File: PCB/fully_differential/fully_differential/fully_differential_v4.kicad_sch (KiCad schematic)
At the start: 35 parts, among them J1 Conn_01x02, J2 Conn_01x03, J3 Conn_01x03, U1 LM324, U2 LM324, U3 LM358, U4 AD8138ARZ, U5 L7805, U6 L7905

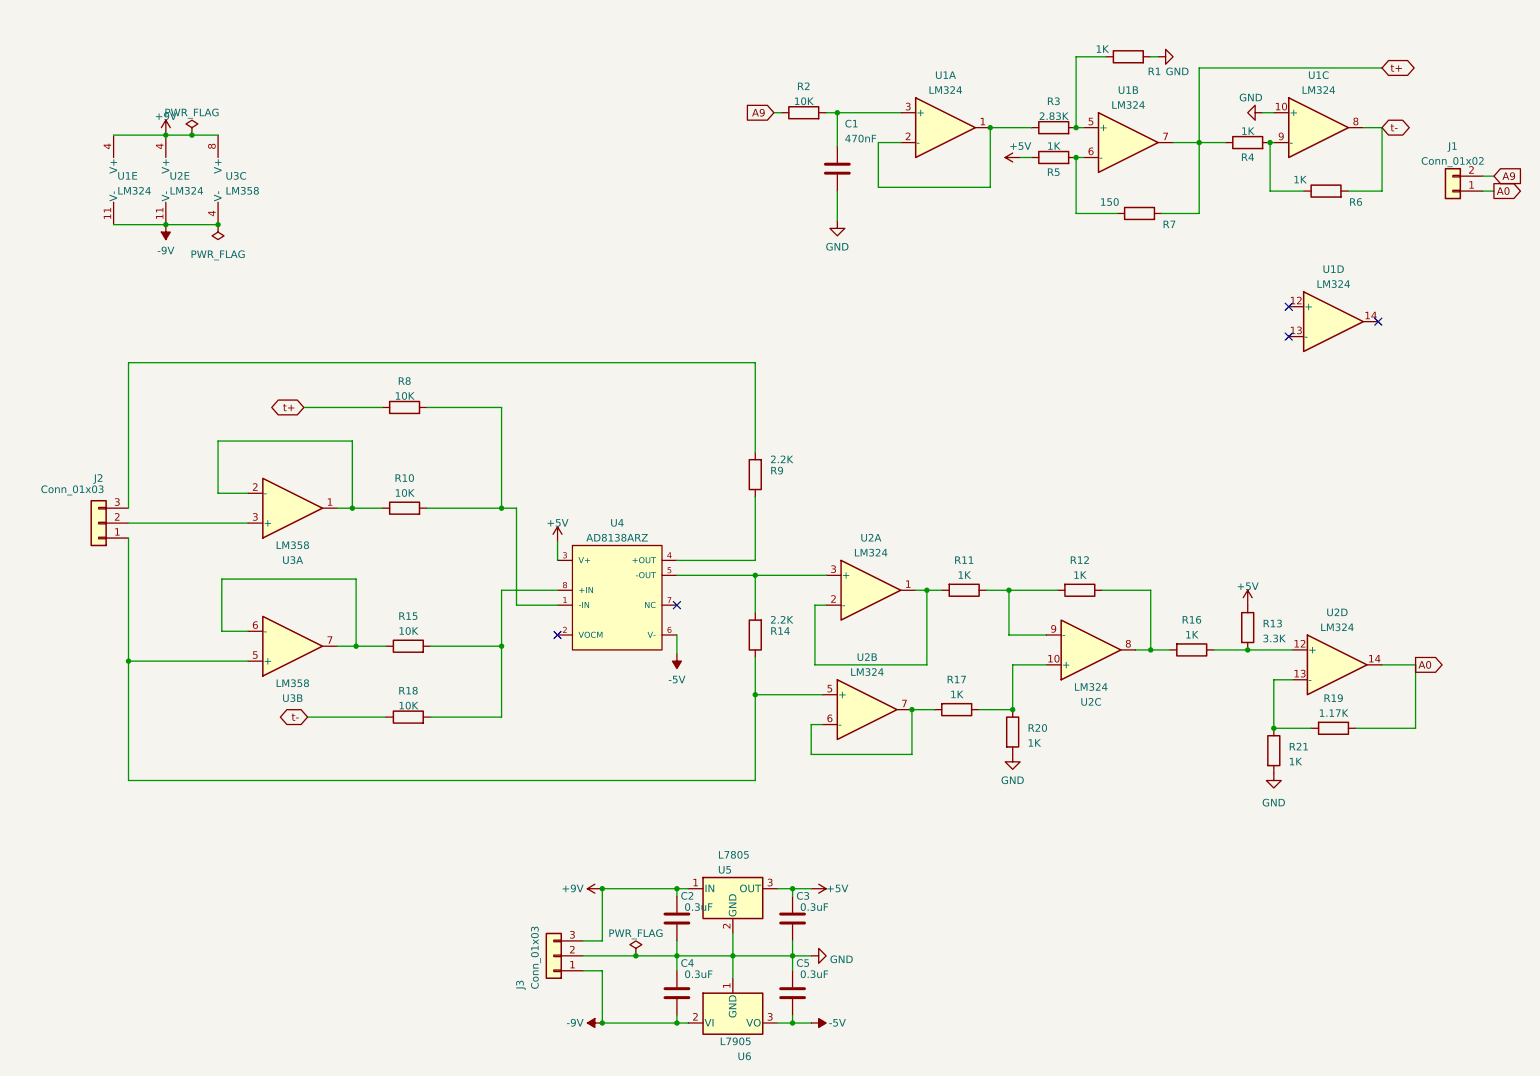
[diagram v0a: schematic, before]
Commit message: fix proteus 1.5v and 3v
stock v2 proteus and kicad ok
fully v4 proteus and kicad ok
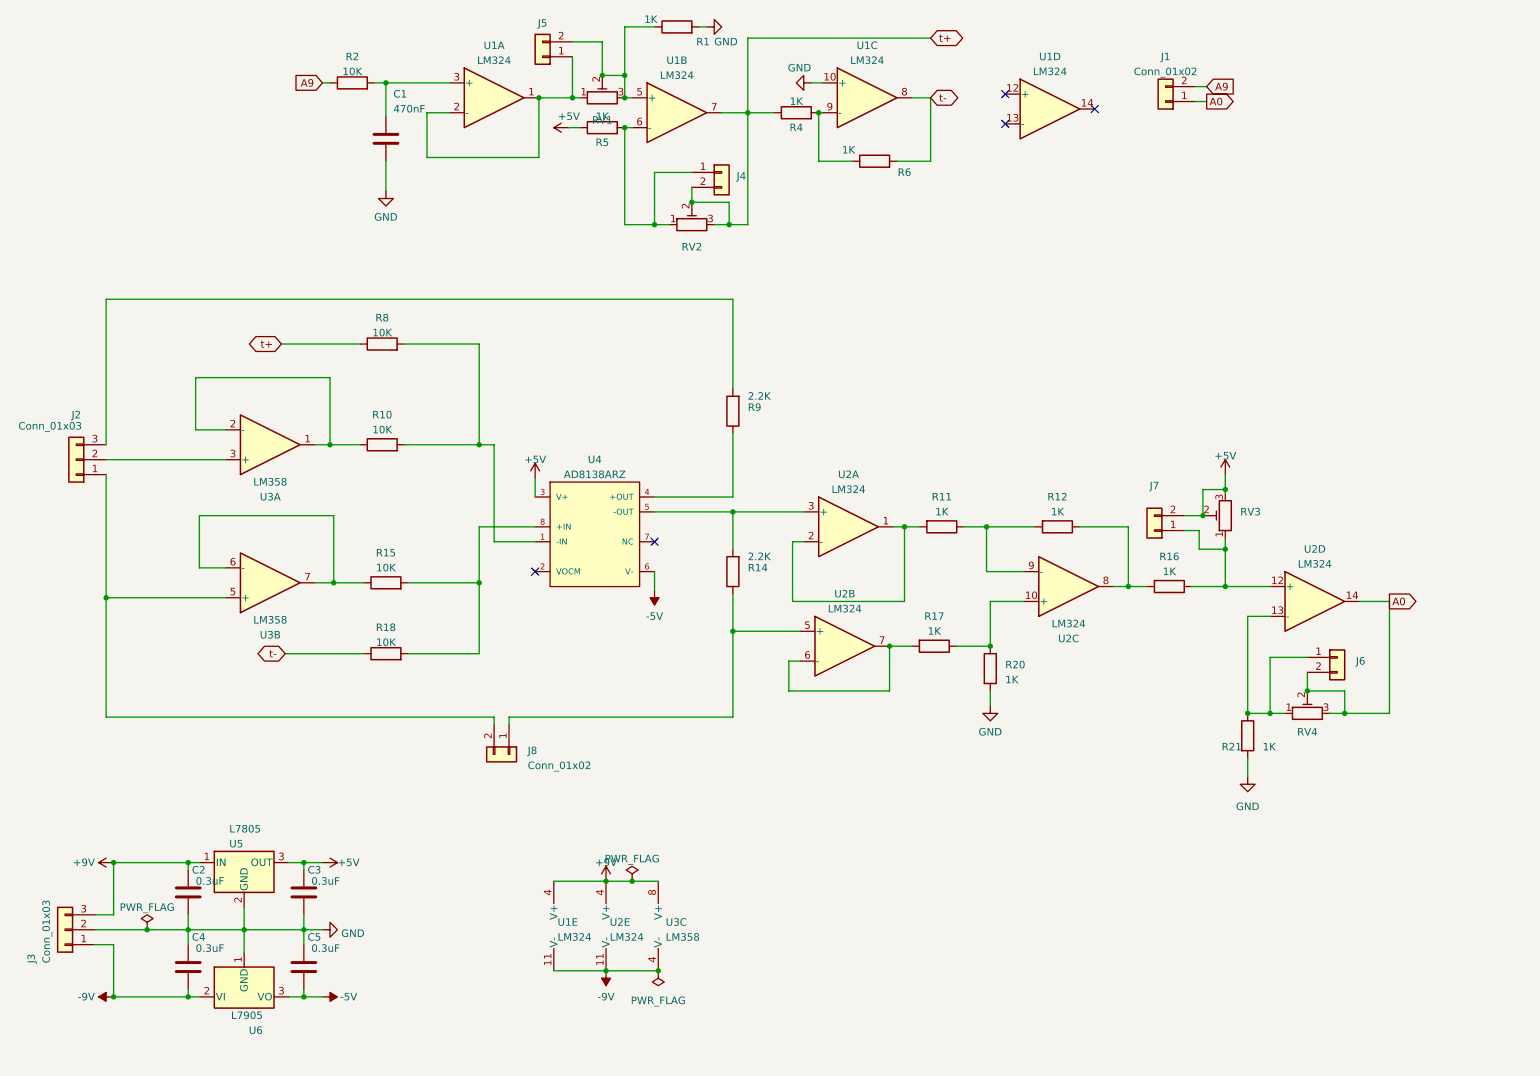
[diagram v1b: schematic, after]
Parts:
- removed R13: 3.3K, Resistor_THT:R_Axial_DIN0207_L6.3mm_D2.5mm_P10.16mm_Horizontal, symbol Device:R
- removed R19: 1.17K, Resistor_THT:R_Axial_DIN0207_L6.3mm_D2.5mm_P10.16mm_Horizontal, symbol Device:R
- removed R3: 2.83K, Resistor_THT:R_Axial_DIN0207_L6.3mm_D2.5mm_P10.16mm_Horizontal, symbol Device:R
- removed R7: 150, Resistor_THT:R_Axial_DIN0207_L6.3mm_D2.5mm_P10.16mm_Horizontal, symbol Device:R
- added J4, J5, J6, J7, J8: Conn_01x02, Connector_PinHeader_2.54mm:PinHeader_1x02_P2.54mm_Vertical, symbol Connector_Generic:Conn_01x02
- added RV1, RV2, RV3, RV4: R_Potentiometer_Trim, Potentiometer_THT:Potentiometer_Bourns_3296W_Vertical, symbol Device:R_Potentiometer_Trim
- J1: footprint Connector_PinSocket_2.54mm:PinSocket_1x02_P2.54mm_Vertical -> Connector_PinHeader_2.54mm:PinHeader_1x02_P2.54mm_Vertical
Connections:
- net +5V: now also J7.2 (Pin_2), RV3.2, RV3.3
- net A0: now also J6.2 (Pin_2), RV4.2, RV4.3
- net t+: now also J4.2 (Pin_2), RV2.2, RV2.3
- net at R16.1, U2.12 (+): now also J7.1 (Pin_1), RV3.1
- net at R21.1, U2.13 (-): now also J6.1 (Pin_1), RV4.1
- net at R5.2, U1.6 (-): now also J4.1 (Pin_1), RV2.1
- net at R1.1, U1.5 (+): now also J5.2 (Pin_2), RV1.2, RV1.3
- net at R14.1, U2.5 (+): now also J8.1 (Pin_1); no longer J2.1 (Pin_1), U3.5 (+)
- net at U1.1, U1.2 (-): now also J5.1 (Pin_1), RV1.1
- new net: J2.1 (Pin_1), J8.2 (Pin_2), U3.5 (+)
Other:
- moved on the sheet: C1, C2, C3, C4, C5, J1, J2, J3, R1, R10, R11, R12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
